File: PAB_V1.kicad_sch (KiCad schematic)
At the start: 17 parts, among them J1 Screw_Terminal_01x02, J2 USB_C_Receptacle_USB2.0_14P, U1 AP63205WU-7, U2 TPS2116DRLR, U3 LM1117MP-3.3

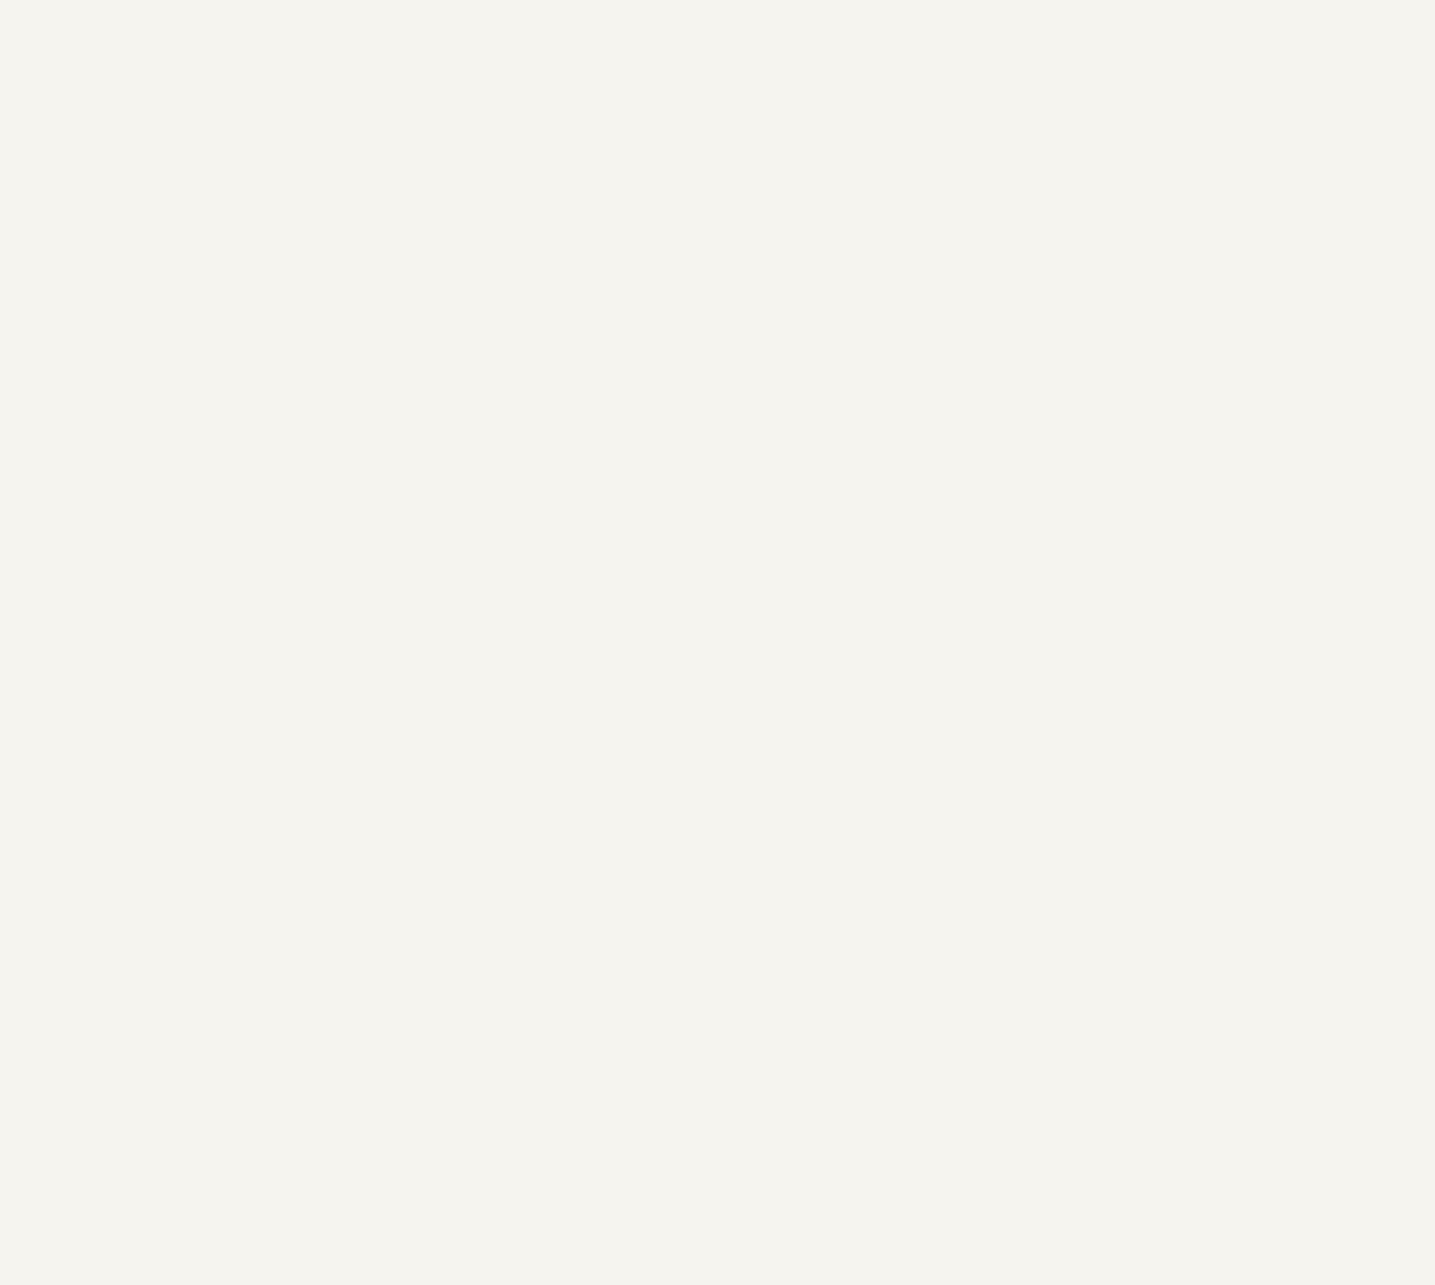
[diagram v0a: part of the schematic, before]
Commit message: Added ESP32-S3FN8, and made some circuitry
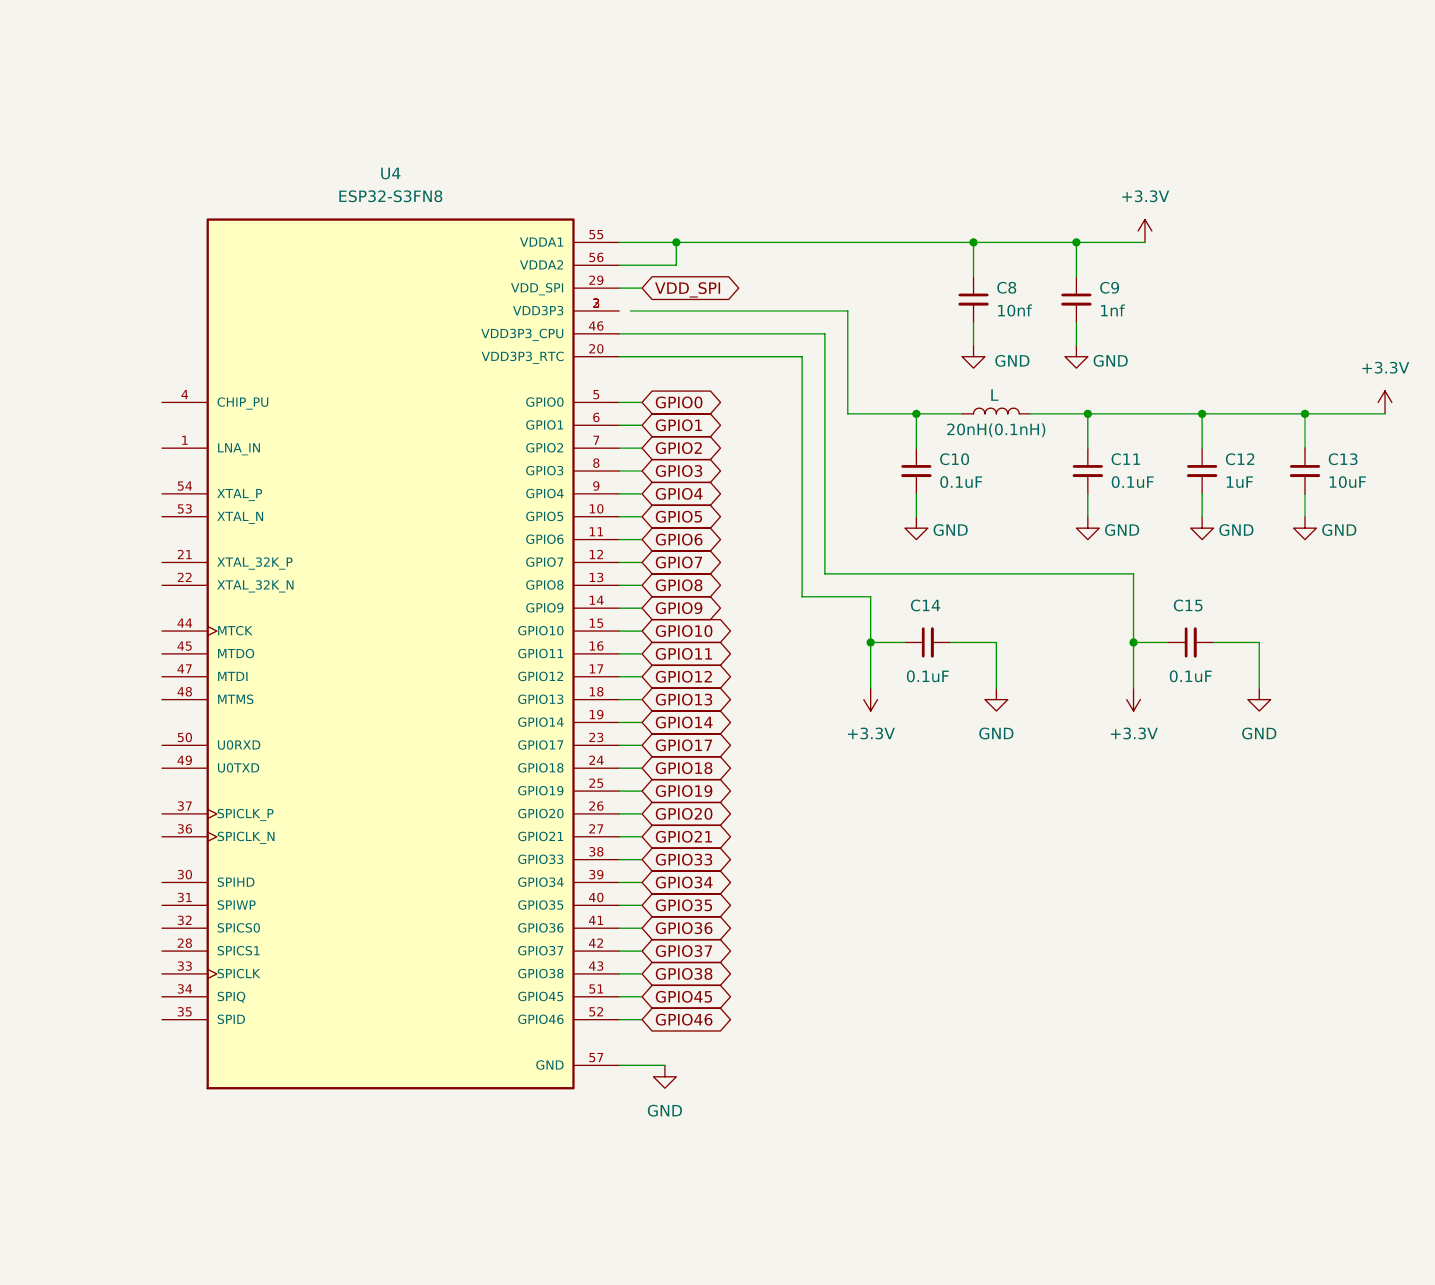
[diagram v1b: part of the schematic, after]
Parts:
- added 20nH(0.1nH): L, symbol Device:L
- added C10, C11, C14, C15: 0.1uF, symbol Device:C_Small
- added C12: 1uF, symbol Device:C_Small
- added C13: 10uF, symbol Device:C_Small
- added C8: 10nf, symbol Device:C_Small
- added C9: 1nf, symbol Device:C_Small
- added U4: ESP32-S3FN8, ESP32-S3FN8:QFN40P700X700X90-57N, symbol ESP32-S3FN8:ESP32-S3FN8
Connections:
- net +3.3V: now also 20nH(0.1nH).2, C11.1, C12.1, C13.1, C14.1, C15.1, C8.1, C9.1, U4.20 (VDD3P3_RTC), U4.46 (VDD3P3_CPU), U4.55 (VDDA1), U4.56 (VDDA2)
- net GND: now also C10.2, C11.2, C12.2, C13.2, C14.2, C15.2, C8.2, C9.2, U4.57 (GND)
- new net: U4.2 (VDD3P3), U4.3 (VDD3P3)
- new net: 20nH(0.1nH).1, C10.1
- new net GPIO0: U4.5 (GPIO0)
- new net GPIO1: U4.6 (GPIO1)
- new net GPIO10: U4.15 (GPIO10)
- new net GPIO11: U4.16 (GPIO11)
- new net GPIO12: U4.17 (GPIO12)
- new net GPIO13: U4.18 (GPIO13)
- new net GPIO14: U4.19 (GPIO14)
- new net GPIO17: U4.23 (GPIO17)
- new net GPIO18: U4.24 (GPIO18)
- new net GPIO19: U4.25 (GPIO19)
- new net GPIO2: U4.7 (GPIO2)
- new net GPIO20: U4.26 (GPIO20)
- new net GPIO21: U4.27 (GPIO21)
- new net GPIO3: U4.8 (GPIO3)
- new net GPIO33: U4.38 (GPIO33)
- new net GPIO34: U4.39 (GPIO34)
- new net GPIO35: U4.40 (GPIO35)
- new net GPIO36: U4.41 (GPIO36)
- new net GPIO37: U4.42 (GPIO37)
- new net GPIO38: U4.43 (GPIO38)
- new net GPIO4: U4.9 (GPIO4)
- new net GPIO45: U4.51 (GPIO45)
- new net GPIO46: U4.52 (GPIO46)
- new net GPIO5: U4.10 (GPIO5)
- new net GPIO6: U4.11 (GPIO6)
- new net GPIO7: U4.12 (GPIO7)
- new net GPIO8: U4.13 (GPIO8)
- new net GPIO9: U4.14 (GPIO9)
- new net VDD_SPI: U4.29 (VDD_SPI)

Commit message: Choose esp32-s3-mini1 instead, and AP63203 as 5V to 3.3V instead ldo converter
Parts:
- removed C6, C7: 10μ *tantalum, symbol Device:C_Small_US
- removed U3: LM1117MP-3.3, Package_TO_SOT_SMD:SOT-223-3_TabPin2, symbol Regulator_Linear:LM1117MP-3.3
- removed U4: ESP32-S3FN8, ESP32-S3FN8:QFN40P700X700X90-57N, symbol ESP32-S3FN8:ESP32-S3FN8
- added C16: 10uF, symbol Device:C_Small
- added C17, C19, C20: 22μF, symbol Device:C_Small
- added C18: 100nf, symbol Device:C_Small
- added L1: 4.7uH, symbol Device:L_Small
- added U3: INTERFACE-CP2102-GMR_QFN28_, INTERFACE-CP2102-GMR_QFN28_:QFN28G_0.5-5X5MM, symbol INTERFACE-CP2102-GMR_QFN28_:INTERFACE-CP2102-GMR_QFN28_
- added U4: AP63203WU, Package_TO_SOT_SMD:TSOT-23-6, symbol Regulator_Switching:AP63203WU
- added U5: ESP32-S3-MINI-1, RF_Module:ESP32-S2-MINI-1, symbol RF_Module:ESP32-S3-MINI-1
- C3: value 2x22μF -> 22μF
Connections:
- net +3.3V: now also C19.1, C20.1, L1.2, U4.1 (FB)
- net +5V: now also C16.1, U4.2 (EN), U4.3 (IN)
- net GND: now also C16.2, C19.2, C20.2, U4.4 (GND)
- new net: C18.1, L1.1, U4.5 (SW)
- new net: C18.2, U4.6 (BST)
- new net: U5.1 (GND), U5.2 (GND), U5.42 (GND), U5.43 (GND), U5.46 (GND), U5.47 (GND), U5.48 (GND), U5.49 (GND), U5.50 (GND), U5.51 (GND), U5.52 (GND), U5.53 (GND), U5.54 (GND), U5.55 (GND), U5.56 (GND), U5.57 (GND), U5.58 (GND), U5.59 (GND), U5.60 (GND), U5.61 (GND), U5.62 (GND), U5.63 (GND), U5.64 (GND), U5.65 (GND)
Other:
- moved on the sheet: 20nH(0.1nH), C10, C11, C12, C13, C14, C15, C8, C9

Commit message: added esp32 and uart circuitry, cleaned chart
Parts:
- removed 20nH(0.1nH): L, symbol Device:L
- removed C10, C11, C14, C15: 0.1uF, symbol Device:C_Small
- removed C12: 1uF, symbol Device:C_Small
- removed C13: 10uF, symbol Device:C_Small
- removed C8: 10nf, symbol Device:C_Small
- removed C9: 1nf, symbol Device:C_Small
- added C21, C23, C24, C6: 0.1uF, symbol Device:C_Small
- added C22: 22μF, symbol Device:C_Small
- added C25, C7: 1uF, symbol Device:C_Small
- added R5: 10 KΩ, symbol Device:R_Small_US
- added R6: 0Ω, symbol Device:R_Small_US
- added SW1: RESET, symbol Switch:SW_Push
- added SW2: BOOT, symbol Switch:SW_Push
- added U6: TPD4E05U06DQAR, TPD4E05U06DQAR:IC_TPD4E05U06DQAR, symbol TPD4E05U06DQAR:TPD4E05U06DQAR
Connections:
- net +3.3V: now also U5.3 (3V3), C22.2, C23.1, R5.2
- net +5V: now also U3.7 (REGIN), U3.8 (VBUS), C6.1, C7.1, U6.1 (D1+)
- net +5V_PS: now also C17.1
- net GND: now also C17.2, U3.3 (GND), U5.1 (GND), U5.2 (GND), U5.42 (GND), U5.43 (GND), U5.46 (GND), U5.47 (GND), U5.48 (GND), U5.49 (GND), U5.50 (GND), U5.51 (GND), U5.52 (GND), U5.53 (GND), U5.54 (GND), U5.55 (GND), U5.56 (GND), U5.57 (GND), U5.58 (GND), U5.59 (GND), U5.60 (GND), U5.61 (GND), U5.62 (GND), U5.63 (GND), U5.64 (GND), U5.65 (GND), C21.1, C22.1, C23.2, C24.2, C25.1, C6.2, C7.2, SW1.1, SW2.1, U6.3 (GND), U6.8 (GND)
- net GPIO1: now also U5.5 (IO1)
- net GPIO10: now also U5.14 (IO10)
- net GPIO11: now also U5.15 (IO11)
- net GPIO12: now also U5.16 (IO12)
- net GPIO13: now also U5.17 (IO13)
- net GPIO14: now also U5.18 (IO14)
- net GPIO17: now also U5.21 (IO17)
- net GPIO18: now also U5.22 (IO18)
- net GPIO2: now also U5.6 (IO2)
- net GPIO21: now also U5.25 (IO21)
- net GPIO3: now also U5.7 (IO3)
- net GPIO33: now also U5.28 (IO33)
- net GPIO34: now also U5.29 (IO34)
- net GPIO35: now also U5.31 (IO35)
- net GPIO36: now also U5.32 (IO36)
- net GPIO37: now also U5.33 (IO37)
- net GPIO38: now also U5.34 (IO38)
- net GPIO4: now also U5.8 (IO4)
- net GPIO45: now also U5.41 (IO45)
- net GPIO46: now also U5.44 (IO46)
- net GPIO5: now also U5.9 (IO5)
- net GPIO6: now also U5.10 (IO6)
- net GPIO7: now also U5.11 (IO7)
- net GPIO8: now also U5.12 (IO8)
- net GPIO9: now also U5.13 (IO9)
- net USB_DN: now also U3.5 (D-), U6.4 (D2+)
- net USB_DP: now also U3.4 (D+), U6.2 (D1-)
- net RXD0: now reaches U3.25 (RXD)
- net RXD0: now also U5.40 (RXD0)
- net TXD0: now reaches U3.26 (TXD)
- net TXD0: now also U5.39 (TXD0)
- net at U3.6 (VDD): now also C21.2
- net GPIO26: now reaches U5.26 (IO26)
- net GPIO47: now reaches U5.27 (IO47)
- net GPIO48: now reaches U5.30 (IO48)
- net at U5.4 (IO0): now also SW2.2
- net EN: now reaches U5.45 (EN)
- net EN: now also C25.2, R5.1, R6.2
- new net: C24.1, R6.1, SW1.2
- no-connect marks 1 -> 35
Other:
- note added: "ESP32-S3-mini1"
- note added: "Uart usb and tvs protection"
- moved on the sheet: 4.7μH, C1, C16, C17, C18, C19, C2, C20, C3, C4, C5, J1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

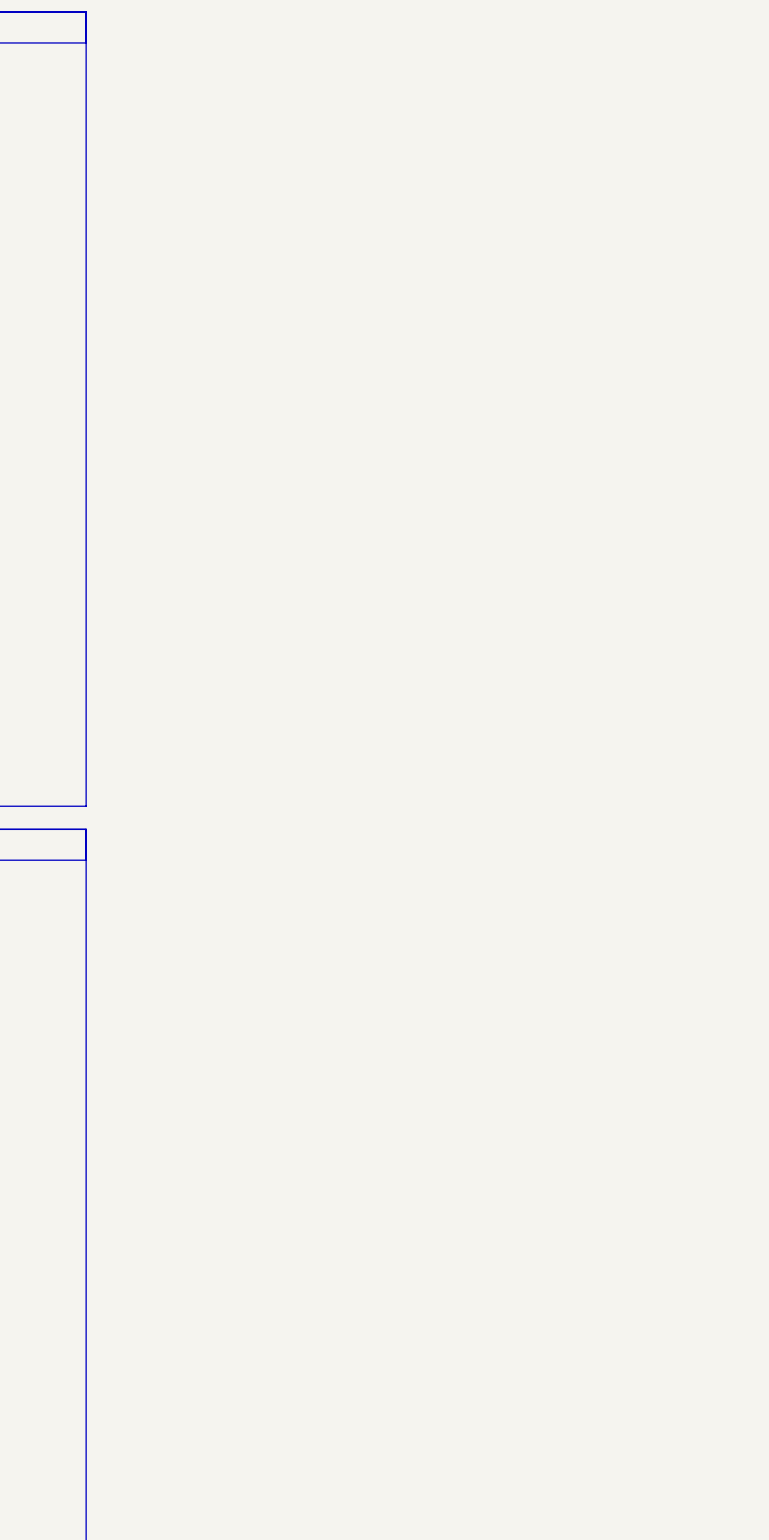
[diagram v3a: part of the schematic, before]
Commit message: Compleated first design, mst be checked and added properly connector
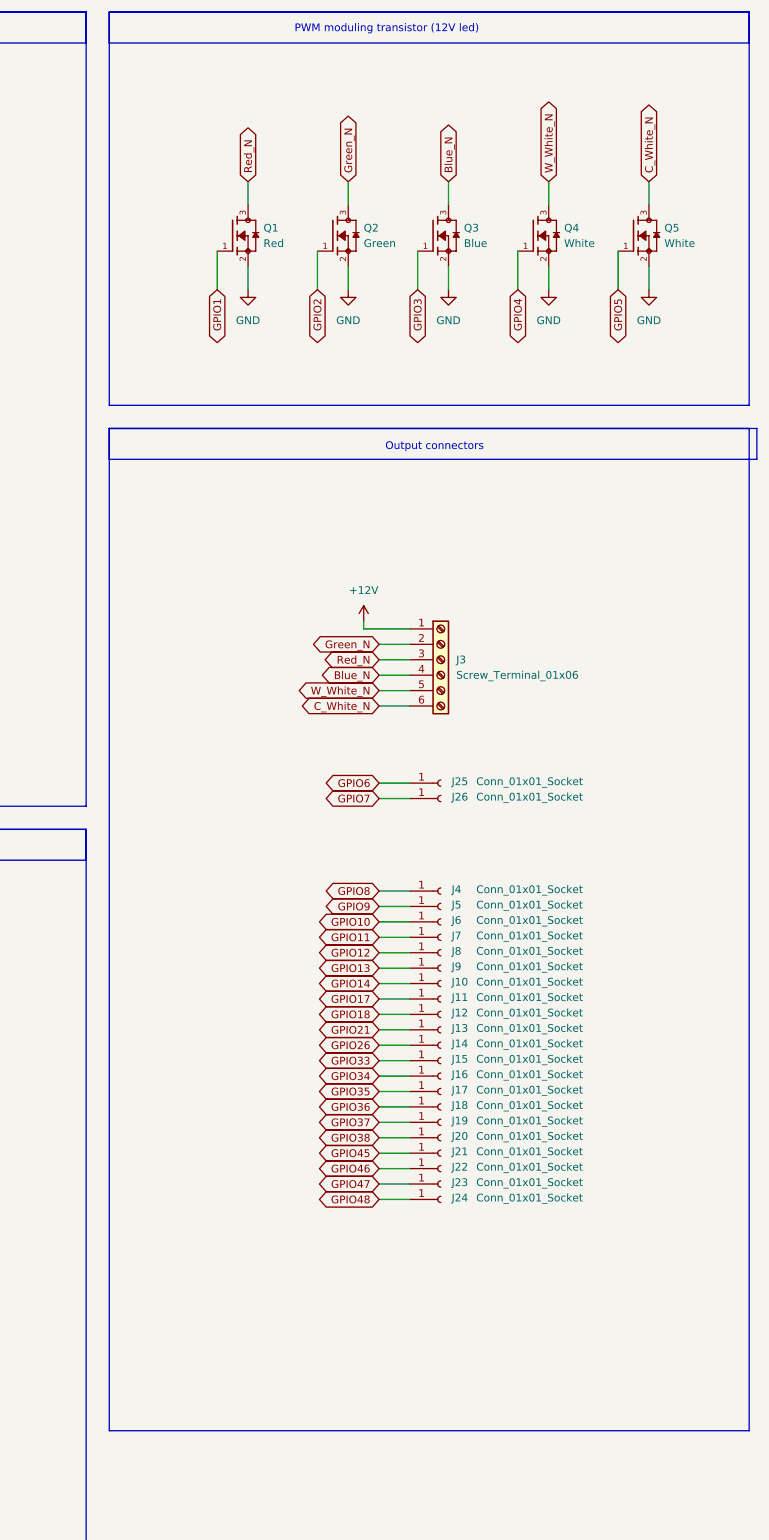
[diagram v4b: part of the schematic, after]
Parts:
- added J10, J11, J12, J13, J14, J15, J16, J17, J18, J19, J20, J21, J22, J23, J24, J25, J26, J4, J5, J6, J7, J8, J9: Conn_01x01_Socket, symbol Connector:Conn_01x01_Socket
- added J3: Screw_Terminal_01x06, symbol Connector:Screw_Terminal_01x06
- added Q1: Red, AO3400A:SOT95P280X125-3N, symbol AO3400A:AO3400A
- added Q2: Green, AO3400A:SOT95P280X125-3N, symbol AO3400A:AO3400A
- added Q3: Blue, AO3400A:SOT95P280X125-3N, symbol AO3400A:AO3400A
- added Q4, Q5: White, AO3400A:SOT95P280X125-3N, symbol AO3400A:AO3400A
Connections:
- net +12V: now also J3.1 (Pin_1)
- net GND: now also Q1.2, Q2.2, Q3.2, Q4.2, Q5.2
- net GPIO1: now also Q1.1
- net GPIO10: now also J6.1 (Pin_1)
- net GPIO11: now also J7.1 (Pin_1)
- net GPIO12: now also J8.1 (Pin_1)
- net GPIO13: now also J9.1 (Pin_1)
- net GPIO14: now also J10.1 (Pin_1)
- net GPIO17: now also J11.1 (Pin_1)
- net GPIO18: now also J12.1 (Pin_1)
- net GPIO2: now also Q2.1
- net GPIO21: now also J13.1 (Pin_1)
- net GPIO26: now also J14.1 (Pin_1)
- net GPIO3: now also Q3.1
- net GPIO33: now also J15.1 (Pin_1)
- net GPIO34: now also J16.1 (Pin_1)
- net GPIO35: now also J17.1 (Pin_1)
- net GPIO36: now also J18.1 (Pin_1)
- net GPIO37: now also J19.1 (Pin_1)
- net GPIO38: now also J20.1 (Pin_1)
- net GPIO4: now also Q4.1
- net GPIO45: now also J21.1 (Pin_1)
- net GPIO46: now also J22.1 (Pin_1)
- net GPIO47: now also J23.1 (Pin_1)
- net GPIO48: now also J24.1 (Pin_1)
- net GPIO5: now also Q5.1
- net GPIO6: now also J25.1 (Pin_1)
- net GPIO7: now also J26.1 (Pin_1)
- net GPIO8: now also J4.1 (Pin_1)
- net GPIO9: now also J5.1 (Pin_1)
- new net Blue_N: J3.4 (Pin_4), Q3.3
- new net C_White_N: J3.6 (Pin_6), Q5.3
- new net Green_N: J3.2 (Pin_2), Q2.3
- new net Red_N: J3.3 (Pin_3), Q1.3
- new net W_White_N: J3.5 (Pin_5), Q4.3
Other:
- note added: "Output connectors"
- note added: "PWM moduling transistor (12V led)"
